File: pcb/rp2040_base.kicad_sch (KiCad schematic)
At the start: 38 parts, among them J0 USB_C_Receptacle_USB2.0, J1 BREAKOUT, J4 Breakout 1.1v, SW0 RESET, SW2 RESET, U2 W25Q128JVS, U3 RP2040, U4 XC6206PxxxMR, U44 SRV05-4, Y0 12MHZ Crystal

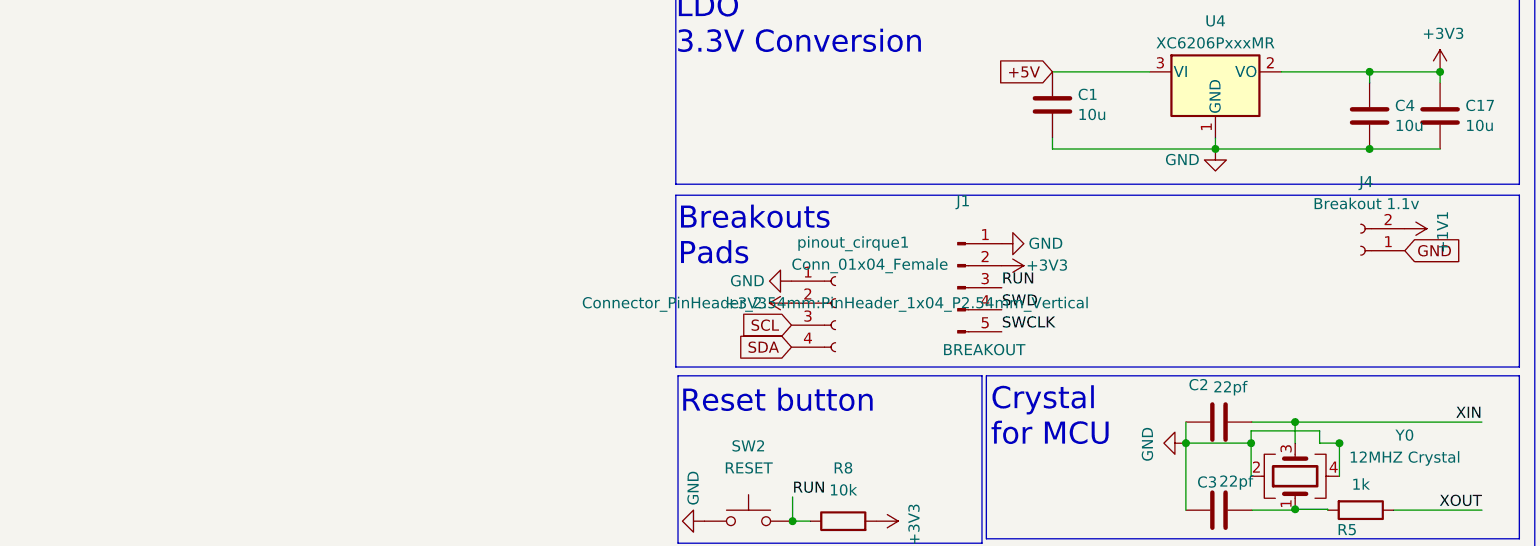
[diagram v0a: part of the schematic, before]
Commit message: add jst and usb breakout support
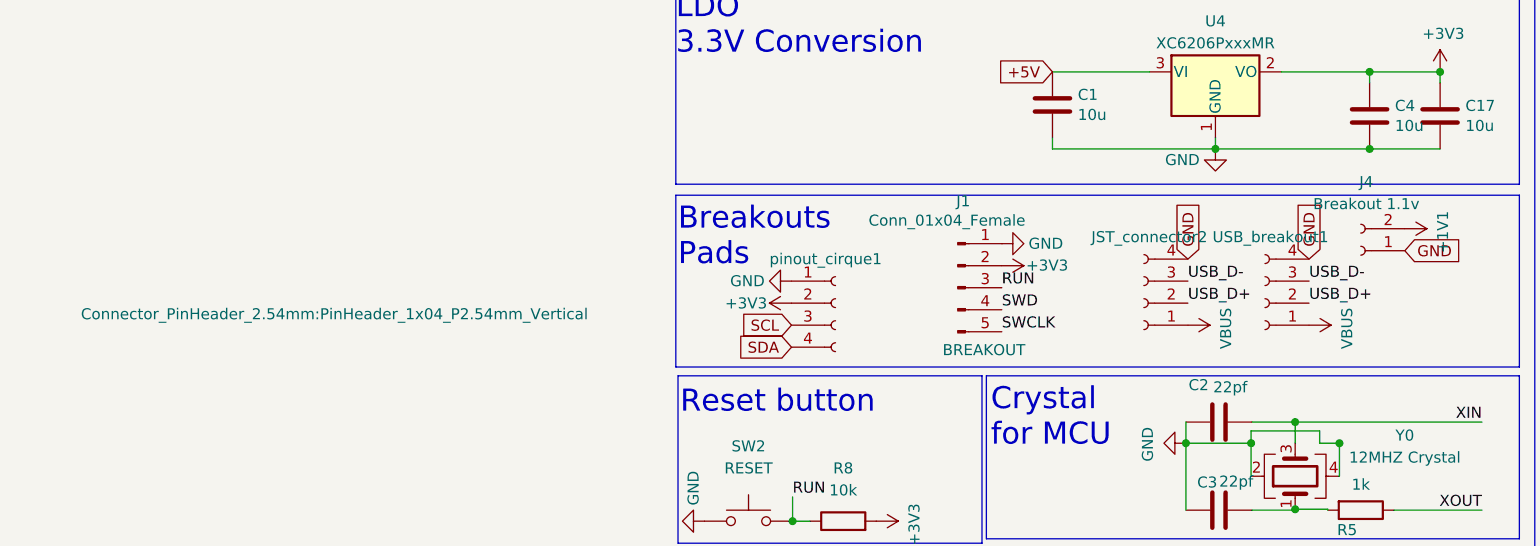
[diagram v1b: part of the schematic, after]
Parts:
- added JST_connector2: Conn_01x04_Female, kbd:Aio3_jst, symbol Connector:Conn_01x04_Female
- added USB_breakout1: Conn_01x04_Female, Connector_PinHeader_2.54mm:PinHeader_1x04_P2.54mm_Vertical, symbol Connector:Conn_01x04_Female
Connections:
- net GND: now also JST_connector2.4 (Pin_4), USB_breakout1.4 (Pin_4)
- net USB_D+: now also JST_connector2.2 (Pin_2), USB_breakout1.2 (Pin_2)
- net USB_D-: now also JST_connector2.3 (Pin_3), USB_breakout1.3 (Pin_3)
- net VBUS: now also JST_connector2.1 (Pin_1), USB_breakout1.1 (Pin_1)
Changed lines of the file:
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@@
+    (effects (font (size 1.27 1.27)) (justify left bottom))
+  )
+  (label "USB_D-" (at 85.725 200.66 0) (fields_autoplaced)
     (effects (font (size 1.27 1.27)) (justify left bottom))
   )
   (label "QSPI_SS" (at 55.118 265.684 0) (fields_autoplaced)
+    (effects (font (size 1.27 1.27)) (justify left bottom))
+  )
+  (label "USB_D+" (at 85.725 203.2 0) (fields_autoplaced)
     (effects (font (size 1.27 1.27)) (justify left bottom))
   )
@@
     (effects (font (size 1.27 1.27)) (justify left bottom))
   )
+  (label "USB_D-" (at 71.755 200.66 0) (fields_autoplaced)
+    (effects (font (size 1.27 1.27)) (justify left bottom))
+  )
   (label "USB_D-" (at 44.45 135.636 0) (fields_autoplaced)
     (effects (font (size 1.27 1.27)) (justify left bottom))
@@
   (label "QSPI_SD0" (at 108.458 263.144 180) (fields_autoplaced)
     (effects (font (size 1.27 1.27)) (justify right bottom))
+  )
+  (label "USB_D+" (at 71.755 203.2 0) (fields_autoplaced)
+    (effects (font (size 1.27 1.27)) (justify left bottom))
   )
   (label "GPIO28_ADC2" (at 240.03 265.938 180) (fields_autoplaced)
@@
     )
   )
+  (global_label "GND" (shape input) (at 71.755 198.12 90) (fields_autoplaced)
+    (effects (font (size 1.27 1.27)) (justify left))
+    (property "Intersheetrefs" "${INTERSHEET_REFS}" (at 71.755 191.2643 90)
+      (effects (font (size 1.27 1.27)) (justify left) hide)
+    )
+  )
   (global_label "+5V" (shape input) (at 87.376 136.398 90) (fields_autoplaced)
     (effects (font (size 1.27 1.27)) (justify left))
@@
     (property "Intersheetrefs" "${INTERSHEET_REFS}" (at 210.1397 123.698 0)
       (effects (font (size 1.27 1.27)) (justify right) hide)
+    )
+  )
+  (global_label "GND" (shape input) (at 85.725 198.12 90) (fields_autoplaced)
+    (effects (font (size 1.27 1.27)) (justify left))
+    (property "Intersheetrefs" "${INTERSHEET_REFS}" (at 85.725 191.2643 90)
+      (effects (font (size 1.27 1.27)) (justify left) hide)
     )
   )
@@
     )
   )
+  (symbol (lib_id "Connector:Conn_01x04_Female") (at 66.675 203.2 180) (unit 1)
+    (in_bom yes) (on_board yes) (dnp no) (fields_autoplaced)
+    (property "Reference" "JST_connector2" (at 67.31 195.58 0)
+      (effects (font (size 1.27 1.27)))
+    )
+    (property "Value" "Conn_01x04_Female" (at 67.31 195.58 0)
+      (effects (font (size 1.27 1.27)) hide)
+    )
+    (property "Footprint" "kbd:Aio3_jst" (at 66.675 203.2 0)
+      (effects (font (size 1.27 1.27)) hide)
+    )
+    (property "Datasheet" "~" (at 66.675 203.2 0)
+      (effects (font (size 1.27 1.27)) hide)
+    )
+    (pin "4")
+    (pin "3")
+    (pin "2")
+    (pin "1")
+    (instances
+      (project "rp2040_base"
+        (path "/2739ccba-417c-4958-a513-8a90d12262a0"
+          (reference "JST_connector2") (unit 1)
+        )
+      )
+    )
+  )
   (symbol (lib_id "Connector:Conn_01x05_Male") (at 45.212 201.422 0) (unit 1)
     (in_bom yes) (on_board yes) (dnp no)
@@
     )
   )
+  (symbol (lib_id "power:VBUS") (at 85.725 205.74 270) (unit 1)
+    (in_bom yes) (on_board yes) (dnp no)
+    (property "Reference" "#PWR015" (at 81.915 205.74 0)
+      (effects (font (size 1.27 1.27)) hide)
+    )
+    (property "Value" "VBUS" (at 90.1192 206.121 0)
+      (effects (font (size 1.27 1.27)))
+    )
+    (property "Footprint" "" (at 85.725 205.74 0)
+      (effects (font (size 1.27 1.27)) hide)
+    )
+    (property "Datasheet" "" (at 85.725 205.74 0)
+      (effects (font (size 1.27 1.27)) hide)
+    )
+    (pin "1")
+    (instances
+      (project "rp2040_base"
+        (path "/2739ccba-417c-4958-a513-8a90d12262a0"
+          (reference "#PWR015") (unit 1)
+        )
+      )
+    )
+  )
   (symbol (lib_id "power:GND") (at 16.002 228.346 270) (unit 1)
     (in_bom yes) (on_board yes) (dnp no)
@@
   (symbol (lib_id "Connector:Conn_01x04_Female") (at 31.115 203.2 0) (unit 1)
     (in_bom yes) (on_board yes) (dnp no)
-    (property "Reference" "pinout_cirque1" (at 26.67 196.215 0)
-      (effects (font (size 1.27 1.27)) (justify left))
-    )
-    (property "Value" "Conn_01x04_Female" (at 26.035 198.755 0)
-      (effects (font (size 1.27 1.27)) (justify left))
-    )
-    (property "Footprint" "Connector_PinHeader_2.54mm:PinHeader_1x04_P2.54mm_Vertical" (at 31.115 203.2 0)
+    (property "Reference" "pinout_cirque1" (at 23.495 198.12 0)
+      (effects (font (size 1.27 1.27)) (justify left))
+    )
+    (property "Value" "Conn_01x04_Female" (at 34.925 193.675 0)
+      (effects (font (size 1.27 1.27)) (justify left))
+    )
+    (property "Footprint" "Connector_PinHeader_2.54mm:PinHeader_1x04_P2.54mm_Vertical" (at -26.67 204.47 0)
       (effects (font (size 1.27 1.27)))
     )
@@
         )
       )
+    )
+  )
+  (symbol (lib_id "power:VBUS") (at 71.755 205.74 270) (unit 1)
+    (in_bom yes) (on_board yes) (dnp no)
+    (property "Reference" "#PWR010" (at 67.945 205.74 0)
+      (effects (font (size 1.27 1.27)) hide)
+    )
+    (property "Value" "VBUS" (at 76.1492 206.121 0)
+      (effects (font (size 1.27 1.27)))
+    )
+    (property "Footprint" "" (at 71.755 205.74 0)
+      (effects (font (size 1.27 1.27)) hide)
+    )
+    (property "Datasheet" "" (at 71.755 205.74 0)
+      (effects (font (size 1.27 1.27)) hide)
+    )
+    (pin "1")
+    (instances
+      (project "rp2040_base"
+        (path "/2739ccba-417c-4958-a513-8a90d12262a0"
+          (reference "#PWR010") (unit 1)
+        )
+      )
+    )
+  )
+  (symbol (lib_id "Connector:Conn_01x04_Female") (at 80.645 203.2 180) (unit 1)
+    (in_bom yes) (on_board yes) (dnp no) (fields_autoplaced)
+    (property "Reference" "USB_breakout1" (at 81.28 195.58 0)
+      (effects (font (size 1.27 1.27)))
+    )
+    (property "Value" "Conn_01x04_Female" (at 81.28 195.58 0)
+      (effects (font (size 1.27 1.27)) hide)
+    )
+    (property "Footprint" "Connector_PinHeader_2.54mm:PinHeader_1x04_P2.54mm_Vertical" (at 80.645 203.2 0)
+      (effects (font (size 1.27 1.27)) hide)
+    )
+    (property "Datasheet" "~" (at 80.645 203.2 0)
+      (effects (font (size 1.27 1.27)) hide)
+    )
+    (pin "4")
+    (pin "3")
+    (pin "2")
+    (pin "1")
+    (instances
+      (project "rp2040_base"
+        (path "/2739ccba-417c-4958-a513-8a90d12262a0"
+          (reference "USB_breakout1") (unit 1)
+        )
+      )
